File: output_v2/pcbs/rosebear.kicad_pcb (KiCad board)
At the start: 2 copper layers, 142.7 x 131.9 mm, 43 parts

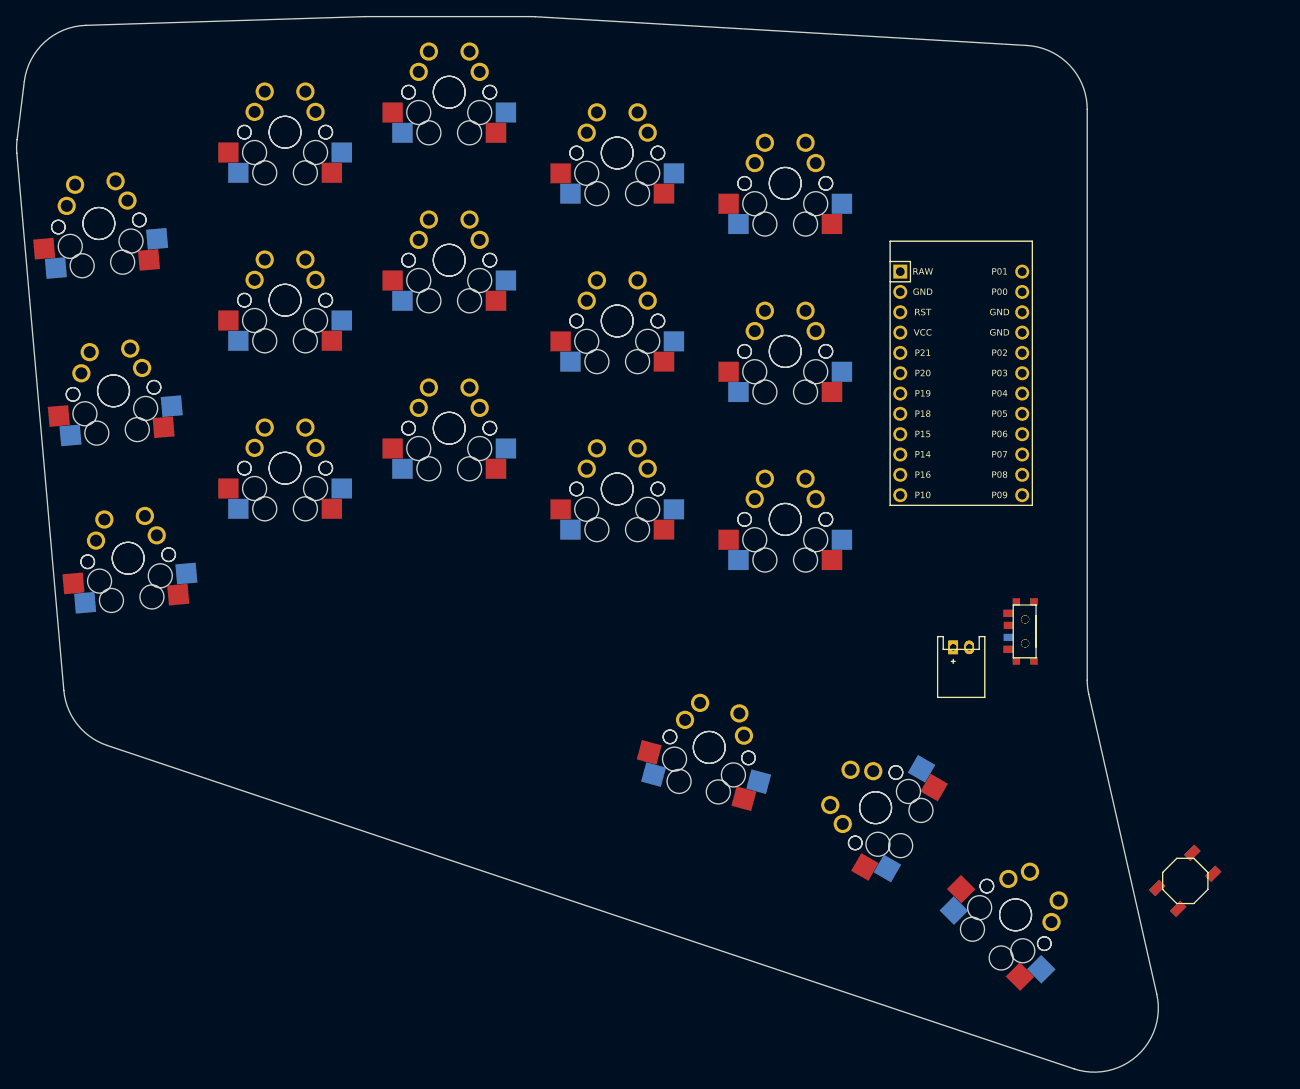
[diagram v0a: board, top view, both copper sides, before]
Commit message: Set up v2 matrix placement board
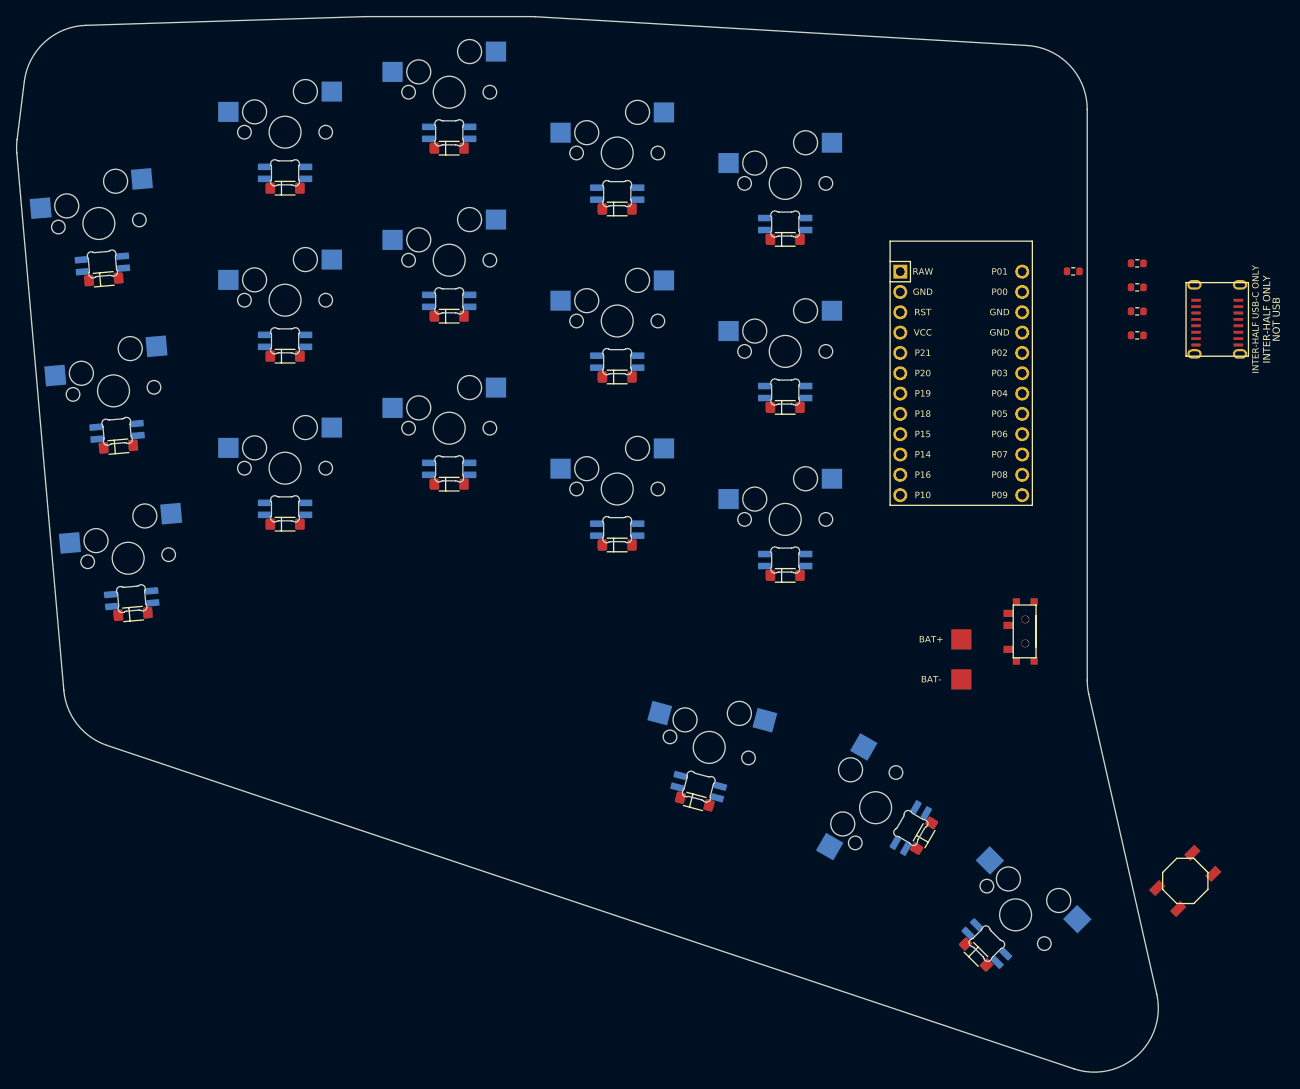
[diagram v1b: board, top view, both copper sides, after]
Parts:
- removed B2: , E73:SW_TACT_ALPS_SKQGABE010
- removed JST1, JST2: , JST_PH_S2B-PH-K_02x2.00mm_Angled
- removed S19, S20, S21, S22, S23, S24, S25, S26, S27, S28, S29, S30, S31, S32, S33, S34, S35, S36: , MX
- removed T2: , E73:SPDT_C128955
- added D1: SOD-123, SOD-123, F.Cu at (50.6, 107.0)
- added D10: SOD-123, SOD-123, F.Cu at (111.1, 98.3)
- added D11: SOD-123, SOD-123, F.Cu at (111.1, 77.3)
- added D12: SOD-123, SOD-123, F.Cu at (111.1, 56.3)
- added D13: SOD-123, SOD-123, F.Cu at (132.1, 102.1)
- added D14: SOD-123, SOD-123, F.Cu at (132.1, 81.1)
- added D15: SOD-123, SOD-123, F.Cu at (132.1, 60.1)
- added D16: SOD-123, SOD-123, F.Cu at (120.8, 130.4)
- added D17: SOD-123, SOD-123, F.Cu at (149.5, 134.7)
- added D18: SOD-123, SOD-123, F.Cu at (156.0, 149.5)
- added D2: SOD-123, SOD-123, F.Cu at (48.8, 86.1)
- added D3: SOD-123, SOD-123, F.Cu at (46.9, 65.1)
- added D4: SOD-123, SOD-123, F.Cu at (69.6, 95.7)
- added D5: SOD-123, SOD-123, F.Cu at (69.6, 74.7)
- added D6: SOD-123, SOD-123, F.Cu at (69.6, 53.7)
- added D7: SOD-123, SOD-123, F.Cu at (90.1, 90.7)
- added D8: SOD-123, SOD-123, F.Cu at (90.1, 69.7)
- added D9: SOD-123, SOD-123, F.Cu at (90.1, 48.7)
- added J1: INTER-HALF USB-C ONLY, USB-C_inter_half_placeholder, F.Cu at (186.1, 70.1)
- added LED1: SK6812MINI-E, SK6812MINI-E_MX-reverse, F.Cu at (50.0, 100.0)
- added LED10: SK6812MINI-E, SK6812MINI-E_MX-reverse, F.Cu at (111.1, 91.3)
- added LED11: SK6812MINI-E, SK6812MINI-E_MX-reverse, F.Cu at (111.1, 70.3)
- added LED12: SK6812MINI-E, SK6812MINI-E_MX-reverse, F.Cu at (111.1, 49.3)
- added LED13: SK6812MINI-E, SK6812MINI-E_MX-reverse, F.Cu at (132.1, 95.1)
- added LED14: SK6812MINI-E, SK6812MINI-E_MX-reverse, F.Cu at (132.1, 74.1)
- added LED15: SK6812MINI-E, SK6812MINI-E_MX-reverse, F.Cu at (132.1, 53.1)
- added LED16: SK6812MINI-E, SK6812MINI-E_MX-reverse, F.Cu at (122.6, 123.6)
- added LED17: SK6812MINI-E, SK6812MINI-E_MX-reverse, F.Cu at (143.4, 131.2)
- added LED18: SK6812MINI-E, SK6812MINI-E_MX-reverse, F.Cu at (160.9, 144.6)
- added LED2: SK6812MINI-E, SK6812MINI-E_MX-reverse, F.Cu at (48.2, 79.1)
- added LED3: SK6812MINI-E, SK6812MINI-E_MX-reverse, F.Cu at (46.3, 58.2)
- added LED4: SK6812MINI-E, SK6812MINI-E_MX-reverse, F.Cu at (69.6, 88.7)
- added LED5: SK6812MINI-E, SK6812MINI-E_MX-reverse, F.Cu at (69.6, 67.7)
- added LED6: SK6812MINI-E, SK6812MINI-E_MX-reverse, F.Cu at (69.6, 46.7)
- added LED7: SK6812MINI-E, SK6812MINI-E_MX-reverse, F.Cu at (90.1, 83.7)
- added LED8: SK6812MINI-E, SK6812MINI-E_MX-reverse, F.Cu at (90.1, 62.7)
- added LED9: SK6812MINI-E, SK6812MINI-E_MX-reverse, F.Cu at (90.1, 41.7)
- added PAD1: , SMDPad, F.Cu at (154.1, 110.1)
- added PAD2: , SMDPad, F.Cu at (154.1, 115.1)
- added R1: R_0603, R_0603_1608Metric, F.Cu at (168.1, 64.1)
- added R2: R_0603, R_0603_1608Metric, F.Cu at (176.1, 63.1)
- added R3: R_0603, R_0603_1608Metric, F.Cu at (176.1, 66.1)
- added R4: R_0603, R_0603_1608Metric, F.Cu at (176.1, 69.1)
- added R5: R_0603, R_0603_1608Metric, F.Cu at (176.1, 72.1)
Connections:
- MCU1 pad 10: P14 -> COL2
- MCU1 pad 11: P16 -> COL3
- MCU1 pad 12: P10 -> COL4
- MCU1 pad 13: P1 -> COL5
- MCU1 pad 14: P0 -> LED_DATA_MCU
- MCU1 pad 17: P2 -> IH_TX_MCU
- MCU1 pad 18: P3 -> IH_RX_MCU
- MCU1 pad 19: P4 -> IH_DETECT_MCU
- MCU1 pad 20: P5 -> IH_SPARE_MCU
- MCU1 pad 21: P6 -> LED_ENABLE
- MCU1 pad 22: P7 -> BATTERY_SENSE
- MCU1 pad 23: P8 -> SPARE_0
- MCU1 pad 24: P9 -> SPARE_1
- MCU1 pad 5: P21 -> ROW0
- MCU1 pad 6: P20 -> ROW1
- MCU1 pad 7: P19 -> ROW2
- MCU1 pad 8: P18 -> COL0
- MCU1 pad 9: P15 -> COL1
- S1 pad 1: P15 -> COL0
- S1 pad 2: GND -> matrix_pinky_bottom_SW
- S10 pad 1: P20 -> COL3
- S10 pad 2: GND -> matrix_index_bottom_SW
- S11 pad 1: P6 -> COL3
- S11 pad 2: GND -> matrix_index_home_SW
- S12 pad 1: P0 -> COL3
- S12 pad 2: GND -> matrix_index_top_SW
- S13 pad 1: P21 -> COL4
- S13 pad 2: GND -> matrix_inner_bottom_SW
- S14 pad 1: P5 -> COL4
- S14 pad 2: GND -> matrix_inner_home_SW
- S15 pad 1: P1 -> COL4
- S15 pad 2: GND -> matrix_inner_top_SW
- S16 pad 1: P14 -> COL5
- S16 pad 2: GND -> thumb_near_thumb_SW
- S17 pad 1: P16 -> COL5
- S17 pad 2: GND -> thumb_home_thumb_SW
- S18 pad 1: P10 -> COL5
- S18 pad 2: GND -> thumb_far_thumb_SW
- S2 pad 1: P9 -> COL0
- S2 pad 2: GND -> matrix_pinky_home_SW
- S3 pad 1: P4 -> COL0
- S3 pad 2: GND -> matrix_pinky_top_SW
- S4 pad 1: P18 -> COL1
- S4 pad 2: GND -> matrix_ring_bottom_SW
- S5 pad 1: P8 -> COL1
- S5 pad 2: GND -> matrix_ring_home_SW
- S6 pad 1: P3 -> COL1
- S6 pad 2: GND -> matrix_ring_top_SW
- S7 pad 1: P19 -> COL2
- S7 pad 2: GND -> matrix_middle_bottom_SW
- S8 pad 1: P7 -> COL2
- S8 pad 2: GND -> matrix_middle_home_SW
- S9 pad 1: P2 -> COL2
- S9 pad 2: GND -> matrix_middle_top_SW
